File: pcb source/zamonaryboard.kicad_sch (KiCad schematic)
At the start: 24 parts, among them J1 USB_C_Receptacle_USB2.0_14P, SW1 SW_Push, U1 ESP32-S2, U2 ME6211C33M5, Y1 Crystal_GND24

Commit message: firmware improvements
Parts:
- removed R6, R7, R8: 0, Resistor_SMD:R_0603_1608Metric, symbol Device:R
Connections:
- net BTN1: now also U1.8 (GPIO3/ADC1_CH2)
- net BTN2: now also U1.10 (GPIO5/ADC1_CH4)
- net at C9.2, Y1.3: now also U1.53 (XTAL_P)

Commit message: v1 commit, desktop app improvements
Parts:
- removed C5: 100nF, Capacitor_SMD:C_0603_1608Metric, symbol Device:C
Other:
- moved on the sheet: C1, C2, C3, C4, C6, C7, SW-RST1, SW1

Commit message: Flipped type-c port and main buttons to the back side, changed reset/boot button to be slimmer, initial new branch commit
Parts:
- SW-RST1, SW1: footprint Button_Switch_SMD:SW_Push_1P1T_NO_6x6mm_H9.5mm -> Button_Switch_SMD:SW_SPST_SKQG_WithoutStem
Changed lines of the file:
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@@
 			)
 		)
-		(property "Footprint" "Button_Switch_SMD:SW_Push_1P1T_NO_6x6mm_H9.5mm"
+		(property "Footprint" "Button_Switch_SMD:SW_SPST_SKQG_WithoutStem"
 			(at 186.69 64.77 0)
 			(effects
@@
 			)
 		)
-		(property "Footprint" "Button_Switch_SMD:SW_Push_1P1T_NO_6x6mm_H9.5mm"
+		(property "Footprint" "Button_Switch_SMD:SW_SPST_SKQG_WithoutStem"
 			(at 81.28 49.53 0)
 			(effects

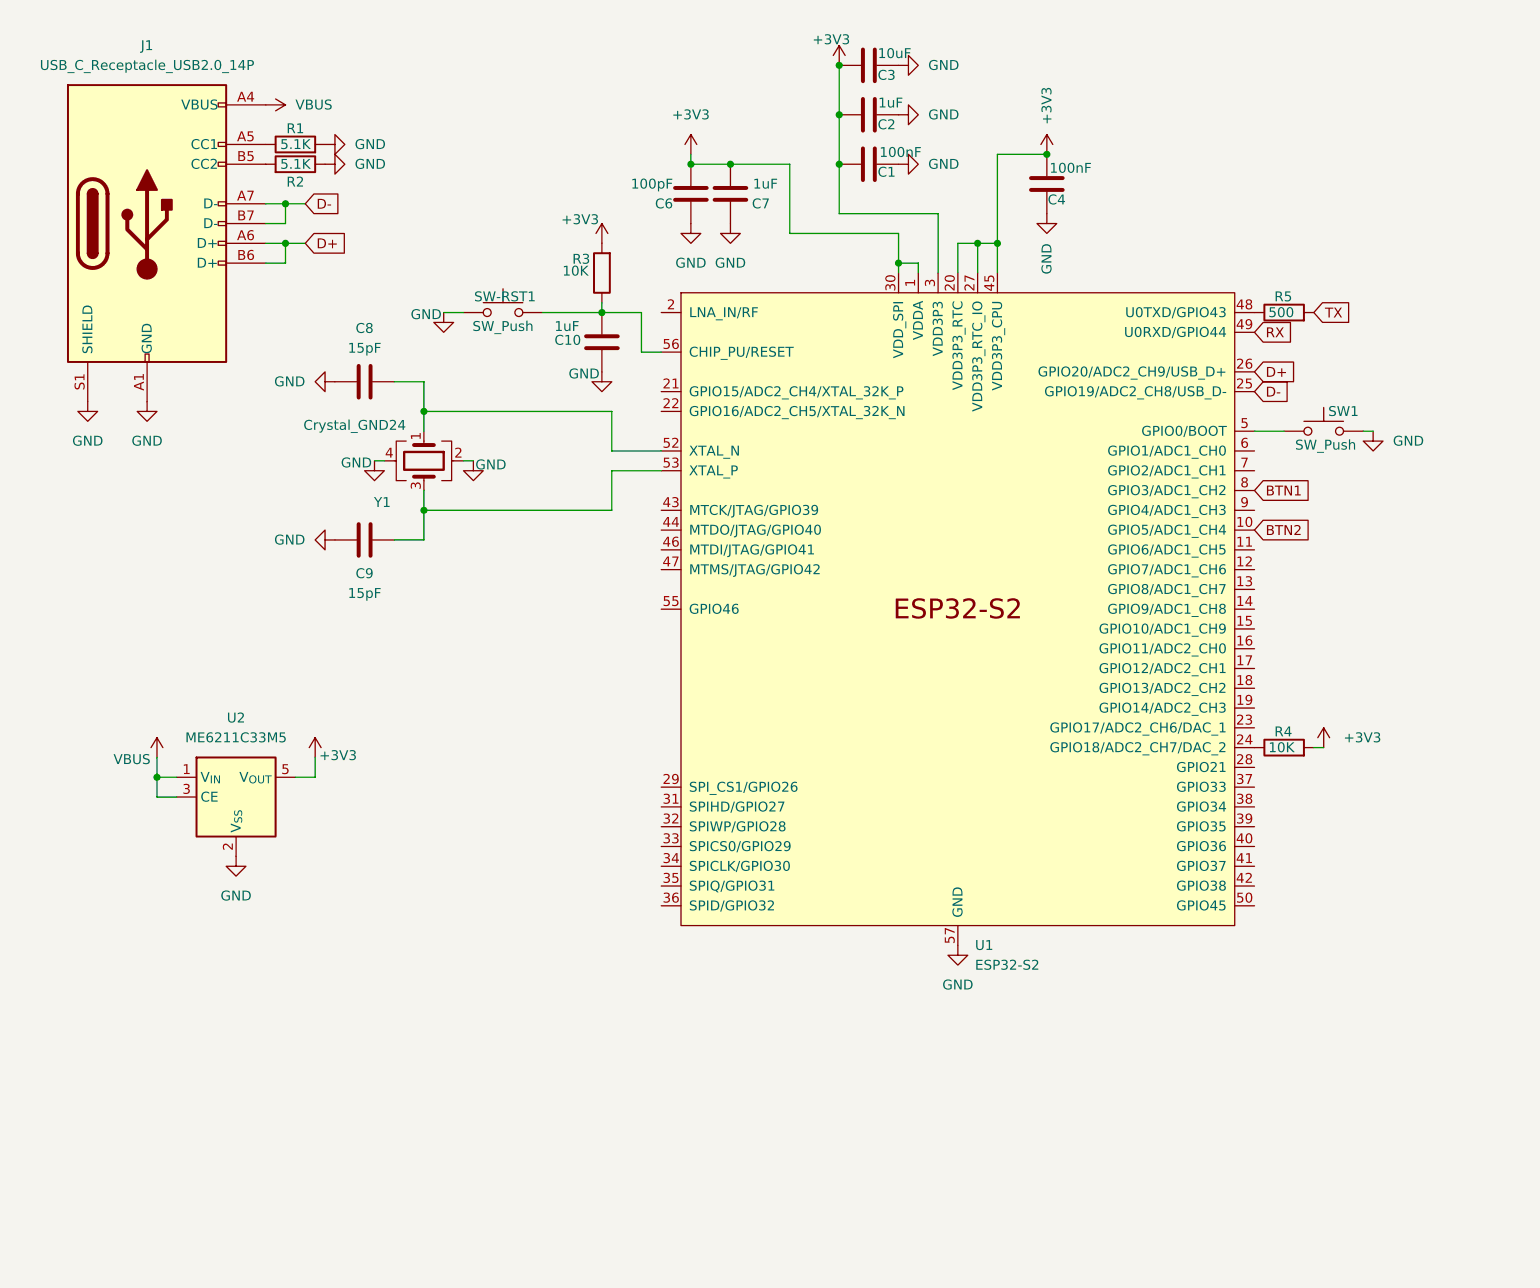
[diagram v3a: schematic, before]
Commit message: WS2812 2020 on the pcb! Not necesseary for proper work
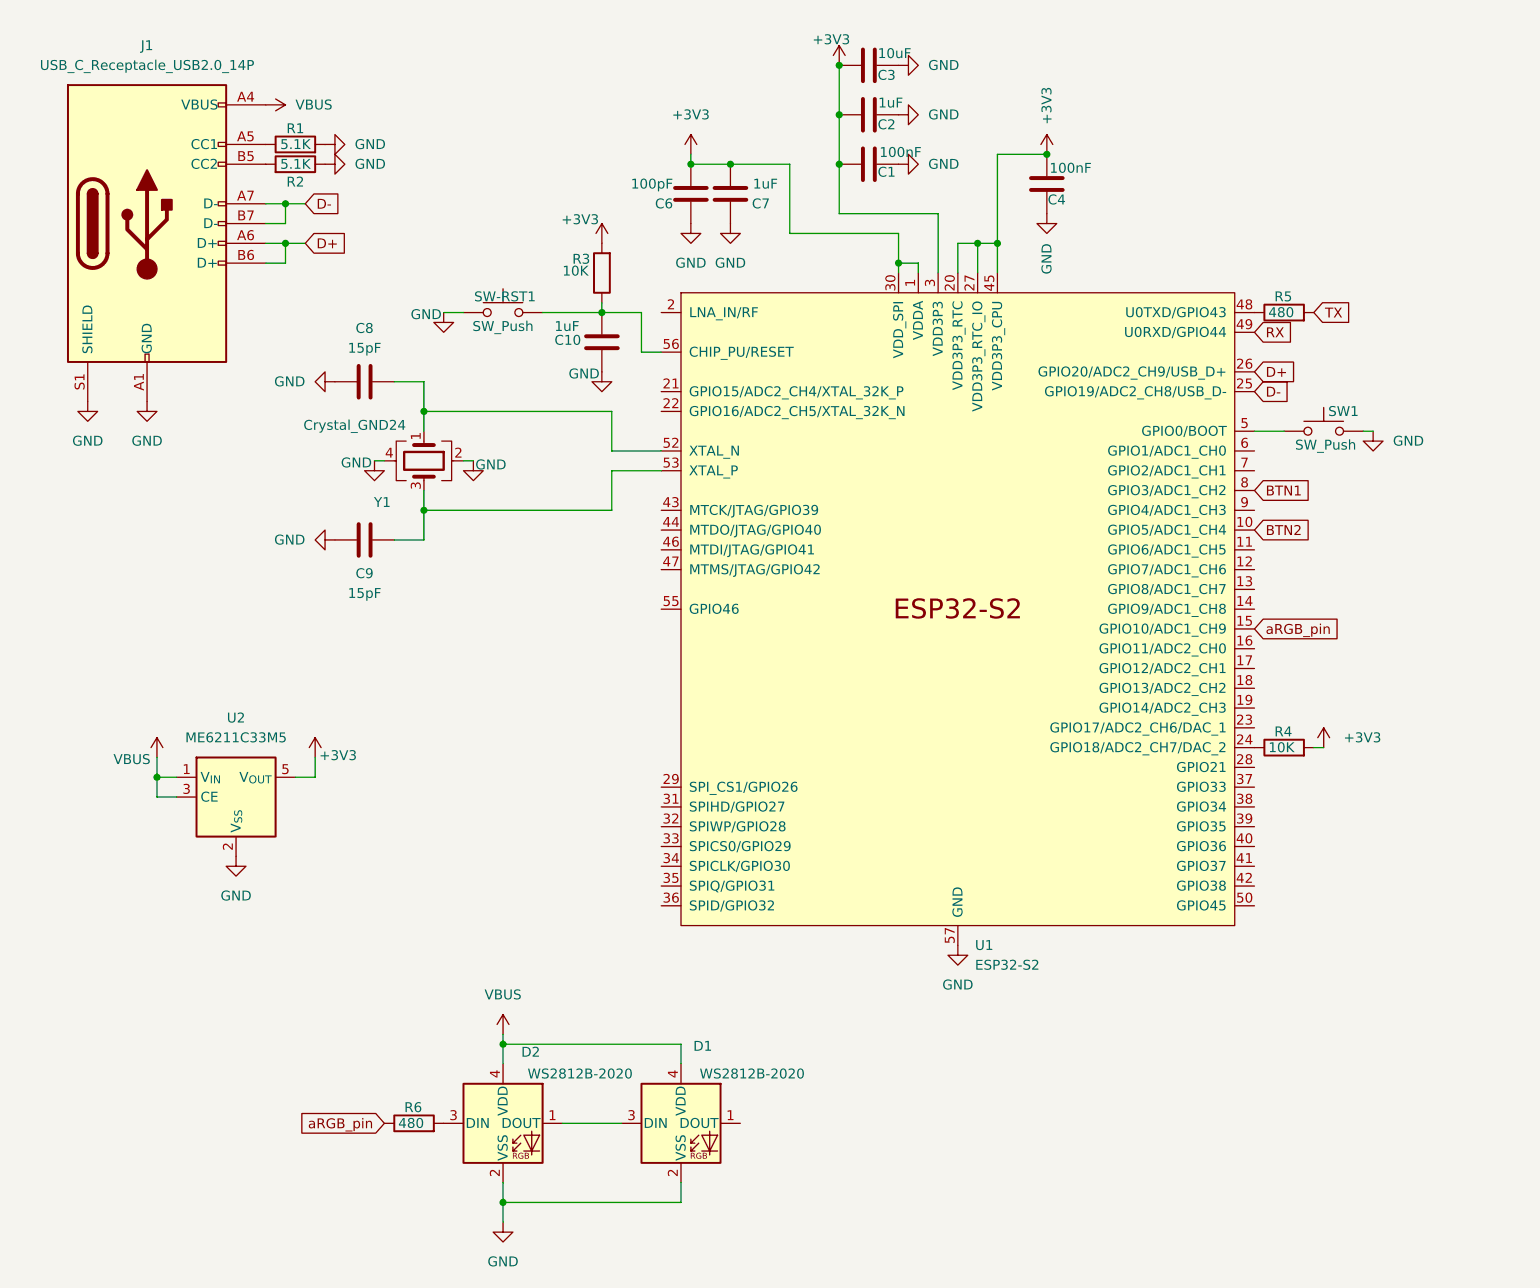
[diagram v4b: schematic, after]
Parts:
- added D1, D2: WS2812B-2020, LED_SMD:LED_WS2812B-2020_PLCC4_2.0x2.0mm, symbol LED:WS2812B-2020
- added R6: 480, Resistor_SMD:R_0603_1608Metric, symbol Device:R
- R5: value 500 -> 480
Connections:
- net GND: now also D1.2 (VSS), D2.2 (VSS)
- net VBUS: now also D1.4 (VDD), D2.4 (VDD)
- net aRGB_pin: now reaches U1.15 (GPIO10/ADC1_CH9)
- net aRGB_pin: now also R6.1
- new net: D1.3 (DIN), D2.1 (DOUT)
- new net: D2.3 (DIN), R6.2

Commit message: v1.2-f, added WS2812-2020 argb leds on the backside of the board (unnecesseary), improvements to pcb routing
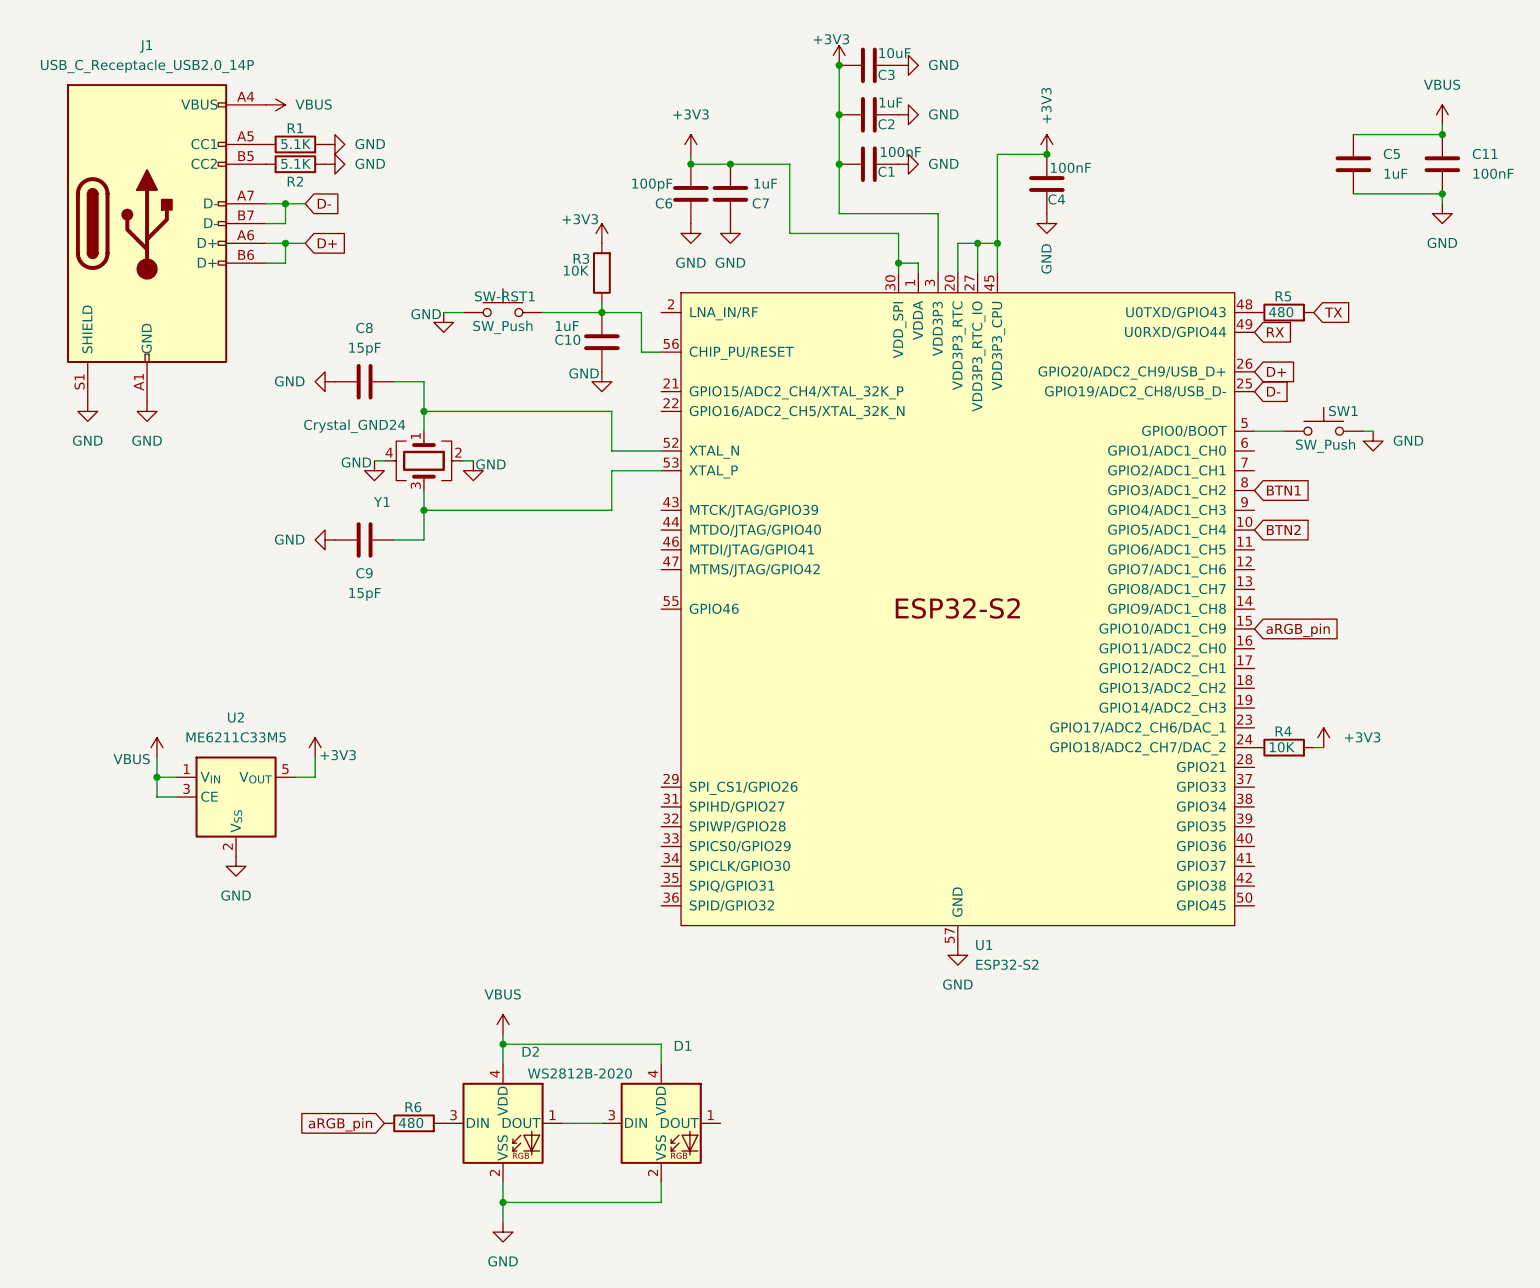
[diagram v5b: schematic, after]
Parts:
- added C11: 100nF, Capacitor_SMD:C_0603_1608Metric, symbol Device:C
- added C5: 1uF, Capacitor_SMD:C_0603_1608Metric, symbol Device:C
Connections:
- net GND: now also C11.2, C5.2
- net VBUS: now also C11.1, C5.1

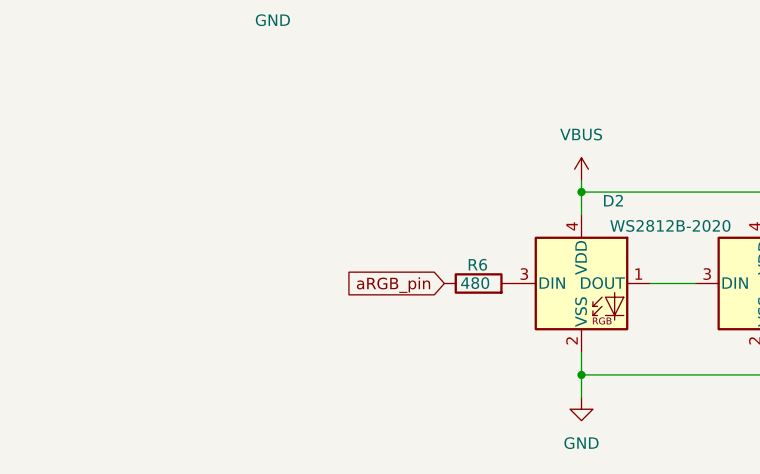
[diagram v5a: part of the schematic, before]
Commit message: Firmware code cleanup, add support for addressible LEDs.
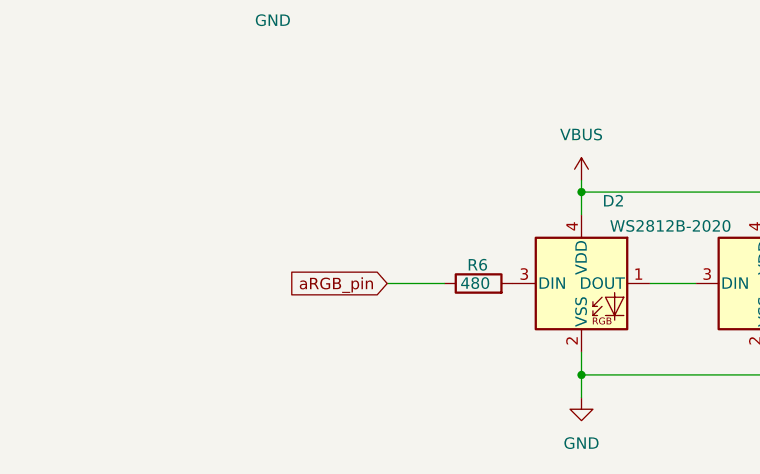
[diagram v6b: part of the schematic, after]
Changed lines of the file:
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@@
+	(wire
+		(pts
+			(xy 59.69 158.75) (xy 66.04 158.75)
+		)
+		(stroke
+			(width 0)
+			(type default)
+		)
+	)
 	(wire
 		(pts
@@
 	(global_label "aRGB_pin"
 		(shape input)
-		(at 66.04 158.75 180)
+		(at 59.69 158.75 180)
 		(fields_autoplaced yes)
 		(effects
@@
 		)
 		(property "Intersheetrefs" "${INTERSHEET_REFS}"
-			(at 54.2254 158.75 0)
+			(at 47.8754 158.75 0)
 			(effects
 				(font
